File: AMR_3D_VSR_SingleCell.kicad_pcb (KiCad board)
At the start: 2 copper layers, 200.8 x 132.1 mm, 39 parts, among them P1 CONN_01X01, P2 CONN_01X01, P3 CONN_02X15, P4 CONN_02X05, P5 CONN_02X02, U1 AFF755b, U10 AFF755b, U11 AFF755b, U12 AFF755b, U13 AFF755b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

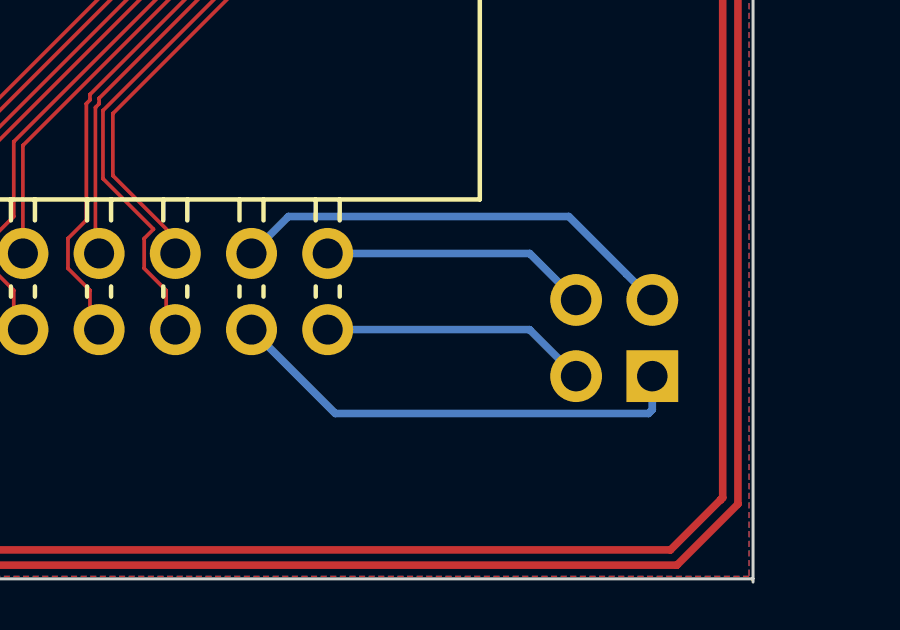
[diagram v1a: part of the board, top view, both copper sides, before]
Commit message: Leiterbahn für die zusätlich load korrigiert.  Committer: Schmitz <ltu@basisit.de>  Changes to be committed: 	modified:   AMR_3D_VSR_SingleCell.kicad_pcb 	modified:   AMR_3D_VSR_SingleCell.kicad_pcb-bak
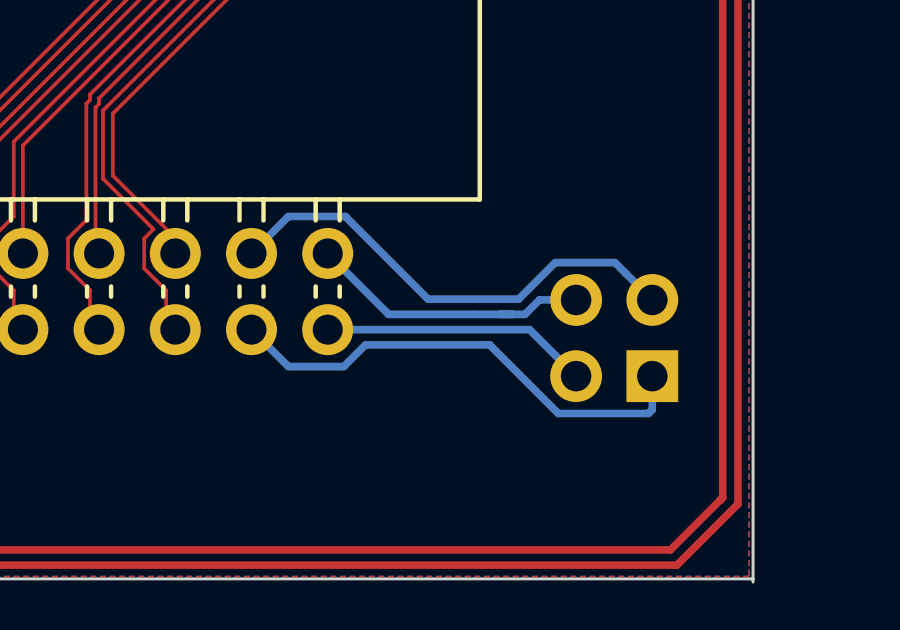
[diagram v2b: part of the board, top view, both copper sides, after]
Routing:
- net Load3: track 26.5 -> 27.5 mm
- net Load4: track 14.3 -> 15.2 mm
- net Load1: track 27.8 -> 28.4 mm
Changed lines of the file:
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@@
 (kicad_pcb (version 4) (host pcbnew 4.0.5)
   (general
-    (links 111)
-    (no_connects 1)
-    (area 109.58097 80.912942 335.522859 273.445)
+    (links 119)
+    (no_connects 5)
+    (area 108.992666 80.912942 335.522859 273.445)
     (thickness 1.6)
     (drawings 60)
-    (tracks 851)
+    (tracks 864)
     (zones 0)
     (modules 39)
@@
   (segment (start 291.82651 210.274896) (end 291.753246 210.34816) (width 0.254) (layer F.Cu) (net 64))
   (segment (start 148.15801 207.78199) (end 150.19 205.75) (width 0.254) (layer F.Cu) (net 64))
-  (segment (start 276.12 204.67) (end 278.914601 207.464601) (width 0.254) (layer B.Cu) (net 65))
-  (segment (start 278.914601 207.464601) (end 289.352999 207.464601) (width 0.254) (layer B.Cu) (net 65))
+  (segment (start 276.12 204.67) (end 277.351001 205.901001) (width 0.254) (layer B.Cu) (net 65))
+  (segment (start 277.351001 205.901001) (end 279.198999 205.901001) (width 0.254) (layer B.Cu) (net 65))
+  (segment (start 279.198999 205.901001) (end 279.92199 205.17801) (width 0.254) (layer B.Cu) (net 65))
+  (segment (start 279.92199 205.17801) (end 284.056 205.17801) (width 0.254) (layer B.Cu) (net 65))
+  (segment (start 284.056 205.17801) (end 286.342591 207.464601) (width 0.254) (layer B.Cu) (net 65))
+  (segment (start 286.342591 207.464601) (end 289.352999 207.464601) (width 0.254) (layer B.Cu) (net 65))
   (segment (start 289.352999 207.464601) (end 289.48 207.3376) (width 0.254) (layer B.Cu) (net 65))
   (segment (start 289.48 207.3376) (end 289.48 206.22) (width 0.254) (layer B.Cu) (net 65))
@@
   (segment (start 165.64948 206.67532) (end 165.64948 205.55772) (width 0.254) (layer B.Cu) (net 65))
   (segment (start 276.12 202.13) (end 277.351001 200.898999) (width 0.254) (layer B.Cu) (net 66))
-  (segment (start 277.351001 200.898999) (end 286.698999 200.898999) (width 0.254) (layer B.Cu) (net 66))
-  (segment (start 286.698999 200.898999) (end 288.616401 202.816401) (width 0.254) (layer B.Cu) (net 66))
+  (segment (start 277.351001 200.898999) (end 279.250881 200.898999) (width 0.254) (layer B.Cu) (net 66))
+  (segment (start 279.250881 200.898999) (end 282.005862 203.65398) (width 0.254) (layer B.Cu) (net 66))
+  (segment (start 282.005862 203.65398) (end 285.026272 203.65398) (width 0.254) (layer B.Cu) (net 66))
+  (segment (start 285.026272 203.65398) (end 286.244853 202.435399) (width 0.254) (layer B.Cu) (net 66))
+  (segment (start 286.244853 202.435399) (end 288.235399 202.435399) (width 0.254) (layer B.Cu) (net 66))
+  (segment (start 288.235399 202.435399) (end 288.616401 202.816401) (width 0.254) (layer B.Cu) (net 66))
   (segment (start 288.616401 202.816401) (end 289.48 203.68) (width 0.254) (layer B.Cu) (net 66))
   (segment (start 155.27 203.21) (end 156.706881 201.773119) (width 0.254) (layer B.Cu) (net 66))
@@
   (segment (start 157.81 205.75) (end 162.9172 205.75) (width 0.254) (layer B.Cu) (net 67))
   (segment (start 162.9172 205.75) (end 163.10948 205.55772) (width 0.254) (layer B.Cu) (net 67))
-  (segment (start 278.66 202.13) (end 285.39 202.13) (width 0.254) (layer B.Cu) (net 68))
-  (segment (start 285.39 202.13) (end 286.94 203.68) (width 0.254) (layer B.Cu) (net 68))
+  (segment (start 283.555 204.16199) (end 284.405 204.16199) (width 0.254) (layer B.Cu) (net 68))
+  (segment (start 284.405 204.16199) (end 284.855 204.16199) (width 0.254) (layer B.Cu) (net 68))
+  (segment (start 286.94 203.68) (end 285.718686 203.68) (width 0.254) (layer B.Cu) (net 68))
+  (segment (start 285.718686 203.68) (end 285.236696 204.16199) (width 0.254) (layer B.Cu) (net 68))
+  (segment (start 285.236696 204.16199) (end 284.405 204.16199) (width 0.254) (layer B.Cu) (net 68))
+  (segment (start 280.69199 204.16199) (end 283.555 204.16199) (width 0.254) (layer B.Cu) (net 68))
+  (segment (start 278.66 202.13) (end 280.69199 204.16199) (width 0.254) (layer B.Cu) (net 68))
   (segment (start 157.81 203.21) (end 162.9172 203.21) (width 0.254) (layer B.Cu) (net 68))
   (segment (start 162.9172 203.21) (end 163.10948 203.01772) (width 0.254) (layer B.Cu) (net 68))
